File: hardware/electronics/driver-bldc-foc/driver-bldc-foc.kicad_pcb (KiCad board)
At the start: 4 copper layers, 80 x 60 mm, 114 parts, among them J1 Conn_01x01_Pin, J10 Conn_01x01_Pin, J11 Conn_01x01_Pin, J12 Conn_01x01_Pin, J13 Conn_01x01_Pin, J14 Conn_01x01_Pin, J15 Conn_01x01_Pin, J16 Conn_01x01_Pin, J17 Conn_01x01_Pin, J18 Conn_01x01_Pin, J19 Conn_01x01_Pin, J2 Conn_01x01_Pin, J20 Conn_01x01_Pin, J21 Conn_01x01_Pin, J22 Conn_01x01_Pin, J3 KH-TYPE-C-16P, J4 Motor_Phase_A, J5 Motor_Phase_B, J6 Motor_Phase_C, J7 Conn_01x04_Pin, J9 Conn_01x01_Pin, Q1 BSC040N10NS5, Q2 BSC040N10NS5, Q3 BSC040N10NS5, Q4 BSC040N10NS5, Q5 BSC040N10NS5, Q6 BSC040N10NS5, U1 TPS563240DDC, U2 STM32G473RETx, U3 AP1117-33, U4 DRV8353RSRGZT, U5 TJA1051T-3, U6 XT30PW-M

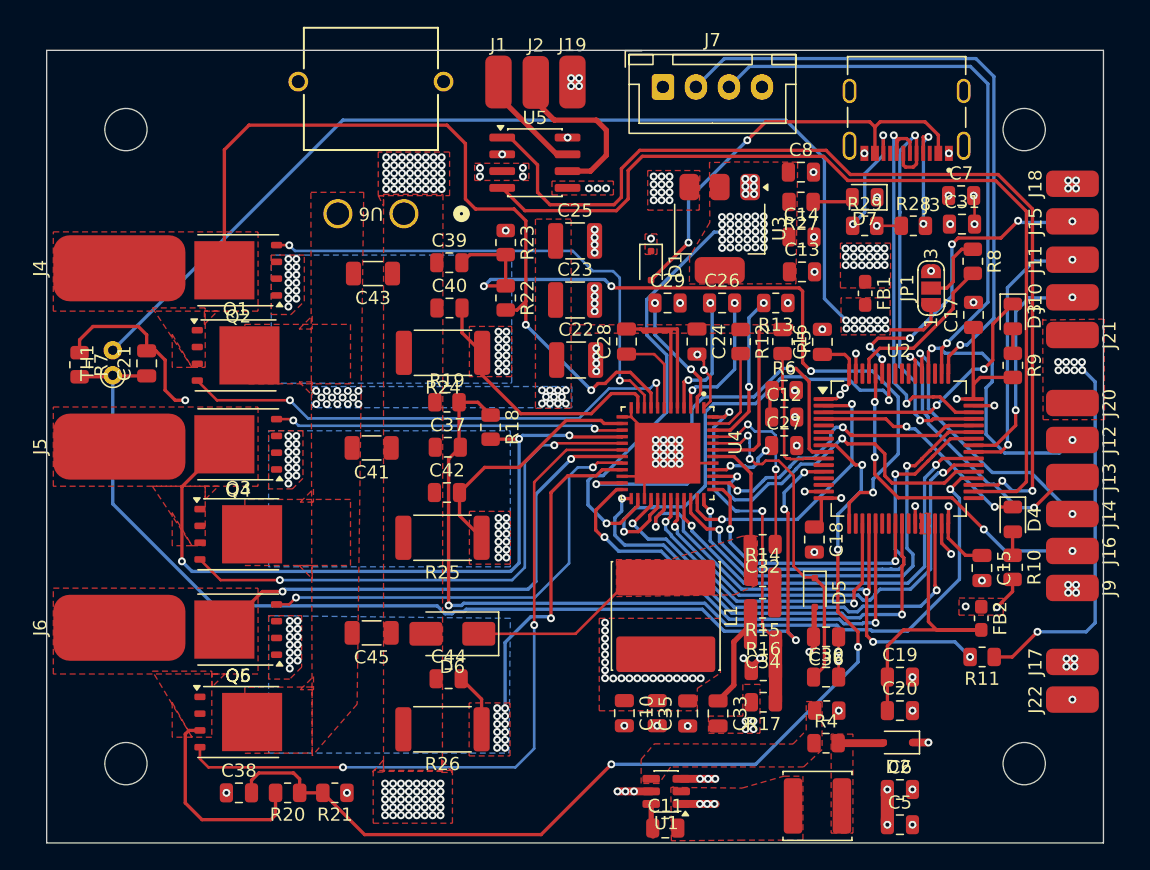
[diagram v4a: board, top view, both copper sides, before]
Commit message: Complete PCB routing, fix net label connections, and export Gerber files for driver-bldc-foc
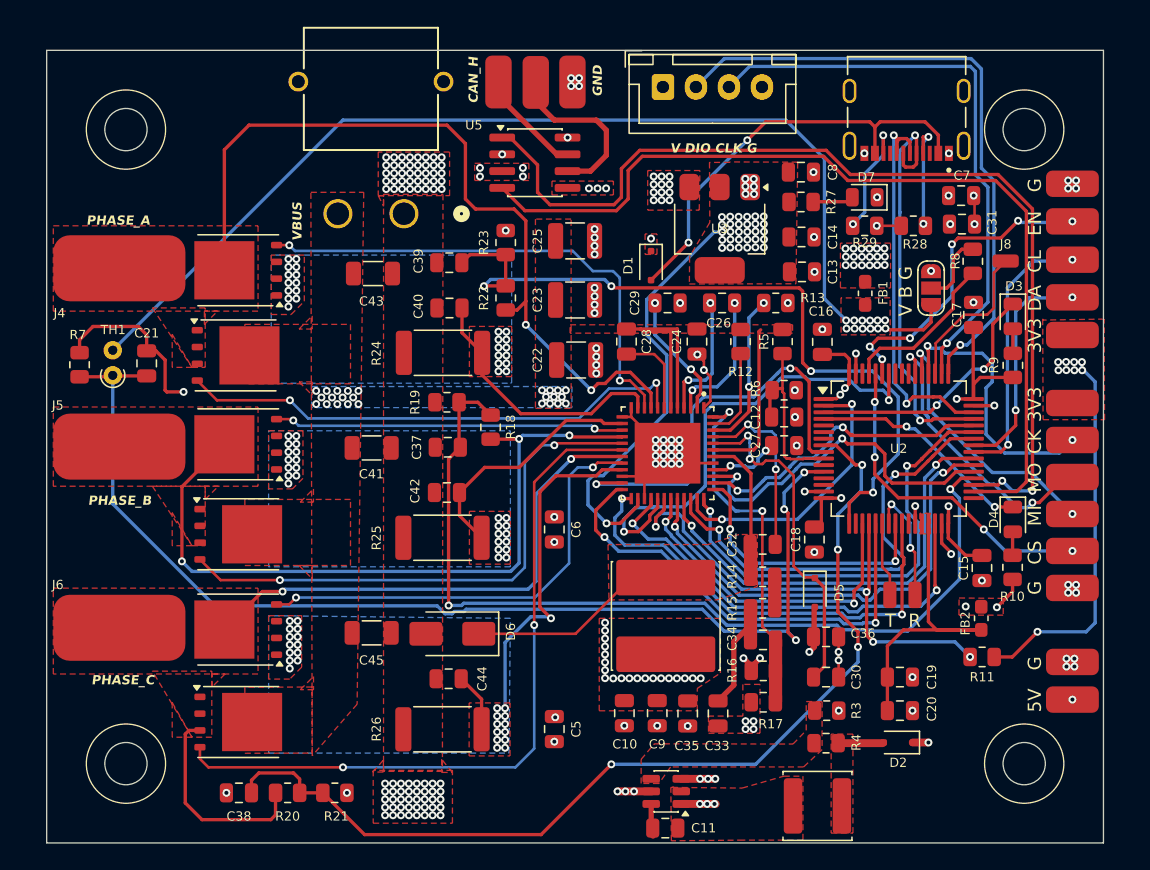
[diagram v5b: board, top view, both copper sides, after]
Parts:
- added J23: Conn_01x01_Pin, Connector_Wire:SolderWirePad_1x01_SMD_1x2mm, F.Cu at (165.7, 141.2)
- added J24: Conn_01x01_Pin, Connector_Wire:SolderWirePad_1x01_SMD_1x2mm, F.Cu at (163.8, 141.2)
- added J8: Conn_01x01_Pin, Connector_Wire:SolderWirePad_1x01_SMD_1x2mm, F.Cu at (172.6, 116.0)
- moved C6 32.7 mm to (138.4, 136.3), turned to 90 degrees
- moved C5 27.1 mm to (138.4, 151.4), turned to -90 degrees
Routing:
- net /MCU/TIM2_CH1: track 0.00 -> 11.8 mm
- net /MCU/U1_RX: track 0.00 -> 9.16 mm, vias 0 -> 2
- net /MCU/U1_TX: track 0.00 -> 5.64 mm
- net +5V: track 3.91 -> 1.25 mm
- net /ThreePhaseBridge and Power/SPC: track 29.4 -> 30.6 mm
- net /MCU/PWM_A+: track 33.7 -> 34.5 mm
- net /MCU/PWM_B+: track 34.0 -> 34.6 mm
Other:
- board text added: "3V3"
- board text added: "5V"
- board text added: "CAN_H"
- board text added: "CK"
- board text added: "CL"
- board text added: "CS"
- board text added: "DA"
- board text added: "EN"
- board text added: "G"
- board text added: "GND"
- board text added: "MI"
- board text added: "MO"
- board text added: "PHASE_A"
- board text added: "PHASE_B"
- board text added: "PHASE_C"
- board text added: "R"
- board text added: "T"
- board text added: "V B G"
- board text added: "V DIO CLK G"
- board text added: "VBUS"
